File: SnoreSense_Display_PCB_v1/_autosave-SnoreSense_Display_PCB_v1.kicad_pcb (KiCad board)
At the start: 2 copper layers, 81 x 60.5 mm, 10 parts, among them J2 JST-PH-2, SW1 SW_Push, SW2 SW_SPDT

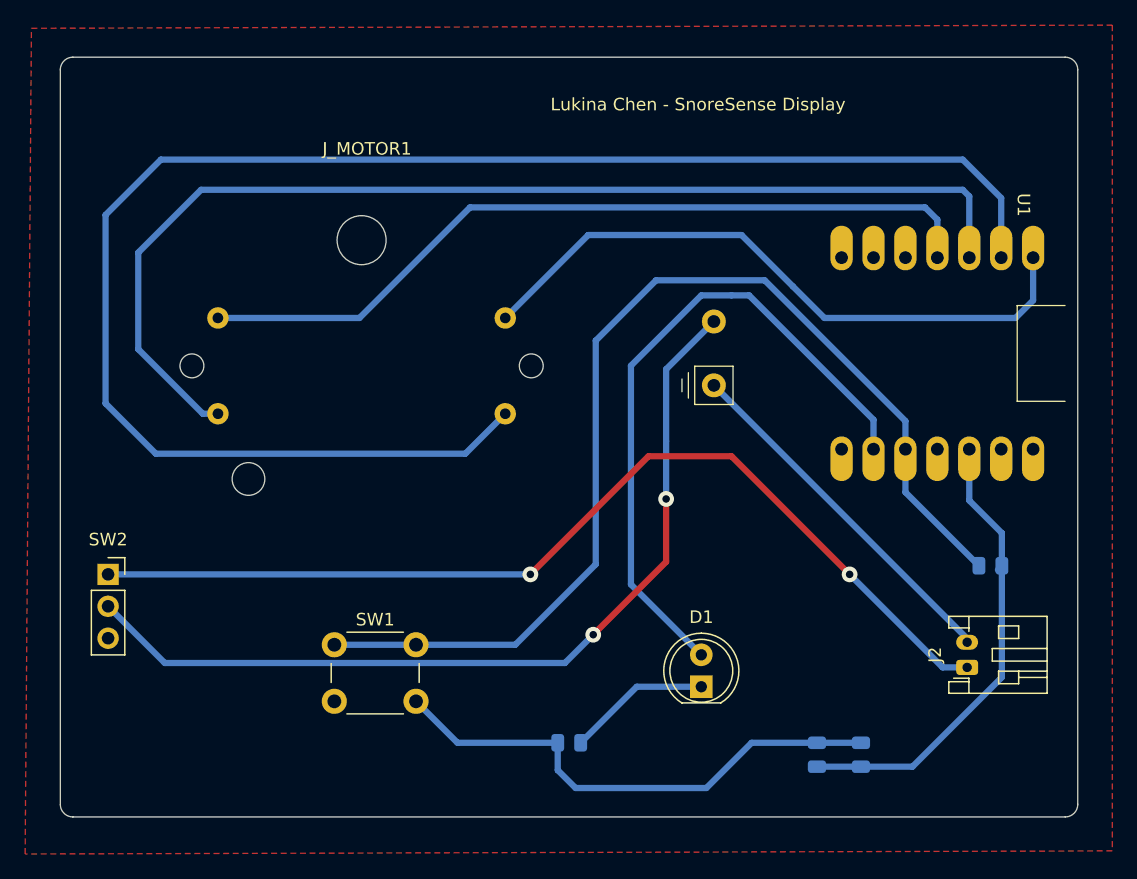
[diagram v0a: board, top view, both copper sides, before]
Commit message: Display code update( now with shorter time for display)
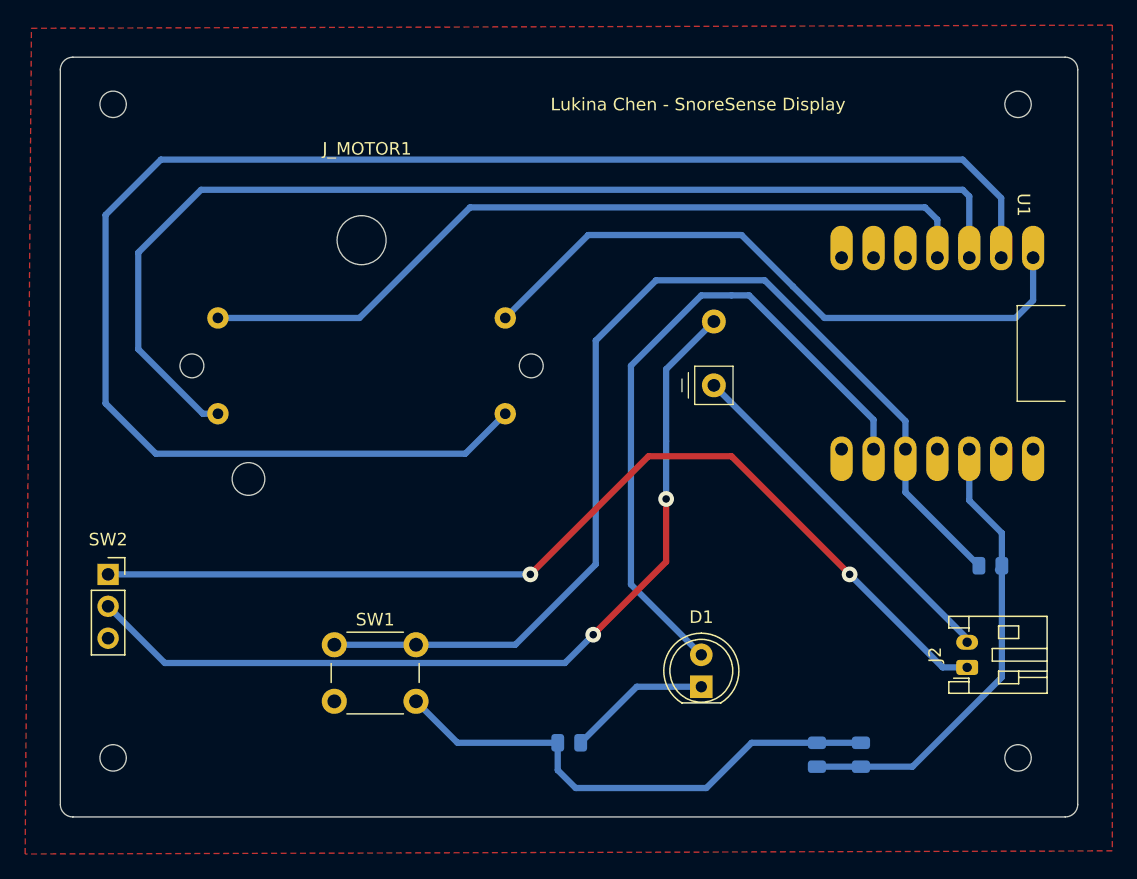
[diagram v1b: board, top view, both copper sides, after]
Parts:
- added REF**: MountingHole_2.1mm, MountingHole:MountingHole_2.1mm, F.Cu at (158.0, 100.0)
- added REF**: MountingHole_2.1mm, MountingHole:MountingHole_2.1mm, F.Cu at (86.0, 100.0)
- added REF**: MountingHole_2.1mm, MountingHole:MountingHole_2.1mm, F.Cu at (86.0, 48.0)
- added REF**: MountingHole_2.1mm, MountingHole:MountingHole_2.1mm, F.Cu at (158.0, 48.0)
